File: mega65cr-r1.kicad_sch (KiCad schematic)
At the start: 0 parts

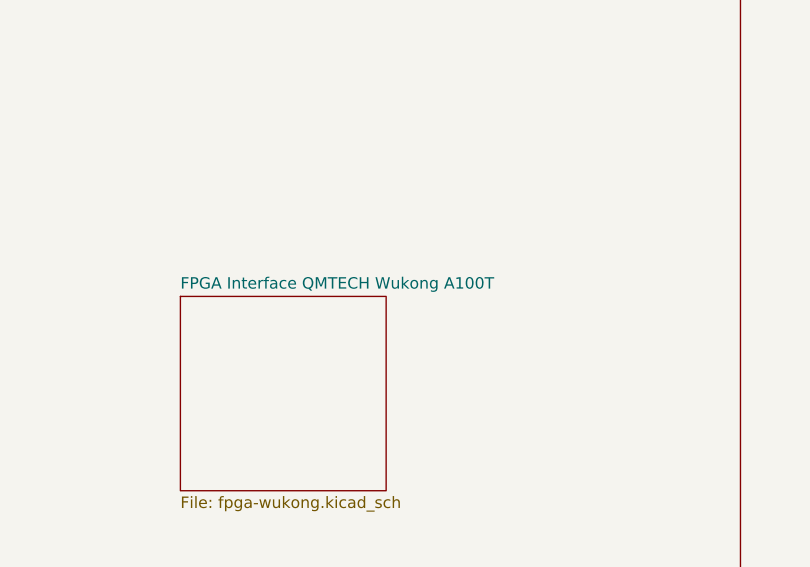
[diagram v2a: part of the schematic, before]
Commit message: add connectors and FPGA pin descriptions for QMTECH K345T board
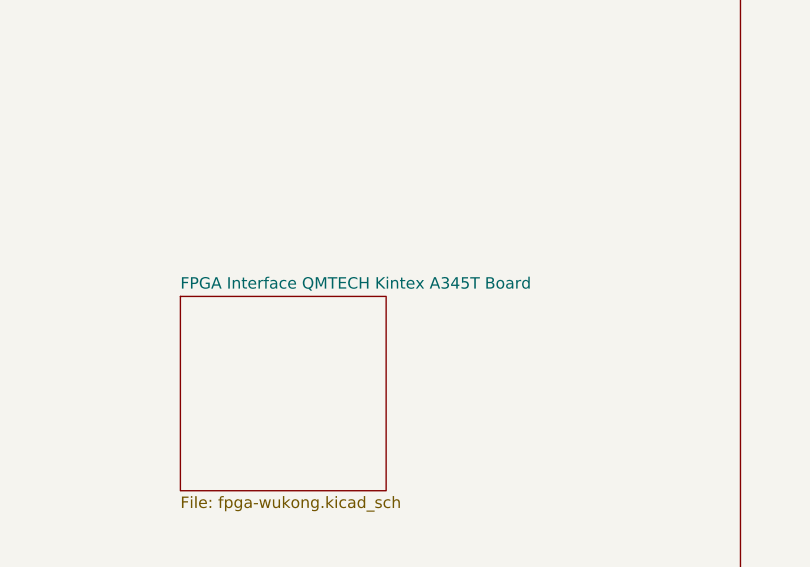
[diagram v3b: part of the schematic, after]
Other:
- sheet FPGA Interface QMTECH Wukong A100T renamed FPGA Interface QMTECH Kintex A345T Board
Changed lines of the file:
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@@
     (stroke (width 0.1524) (type solid) (color 0 0 0 0))
     (fill (color 0 0 0 0.0000))
-    (property "Sheet name" "FPGA Interface QMTECH Wukong A100T" (id 0) (at 104.14 74.2184 0)
+    (property "Sheet name" "FPGA Interface QMTECH Kintex A345T Board" (id 0) (at 104.14 74.2184 0)
       (effects (font (size 1.27 1.27)) (justify left bottom))
     )
@@
       (reference "J2") (unit 1) (value "DB9_Male_MountingHoles") (footprint "Connector_Dsub:DSUB-9_Male_Horizontal_P2.77x2.84mm_EdgePinOffset7.70mm_Housed_MountingHolesOffset9.12mm")
     )
+    (path "/2879178d-3b15-409b-b355-34424f0e3bd8/24d8d35c-436f-43c1-9f20-ff6b2f007989"
+      (reference "J4") (unit 1) (value "Conn_02x32_Odd_Even") (footprint "")
+    )
+    (path "/2879178d-3b15-409b-b355-34424f0e3bd8/4e0105b8-2efd-42c5-8acf-67155eec9ca7"
+      (reference "J5") (unit 1) (value "Conn_02x32_Odd_Even") (footprint "")
+    )
     (path "/bf6f0944-6234-4b84-bc75-6d48246ce101/9b2913aa-2e6f-4a94-a0c7-53573f96600d"

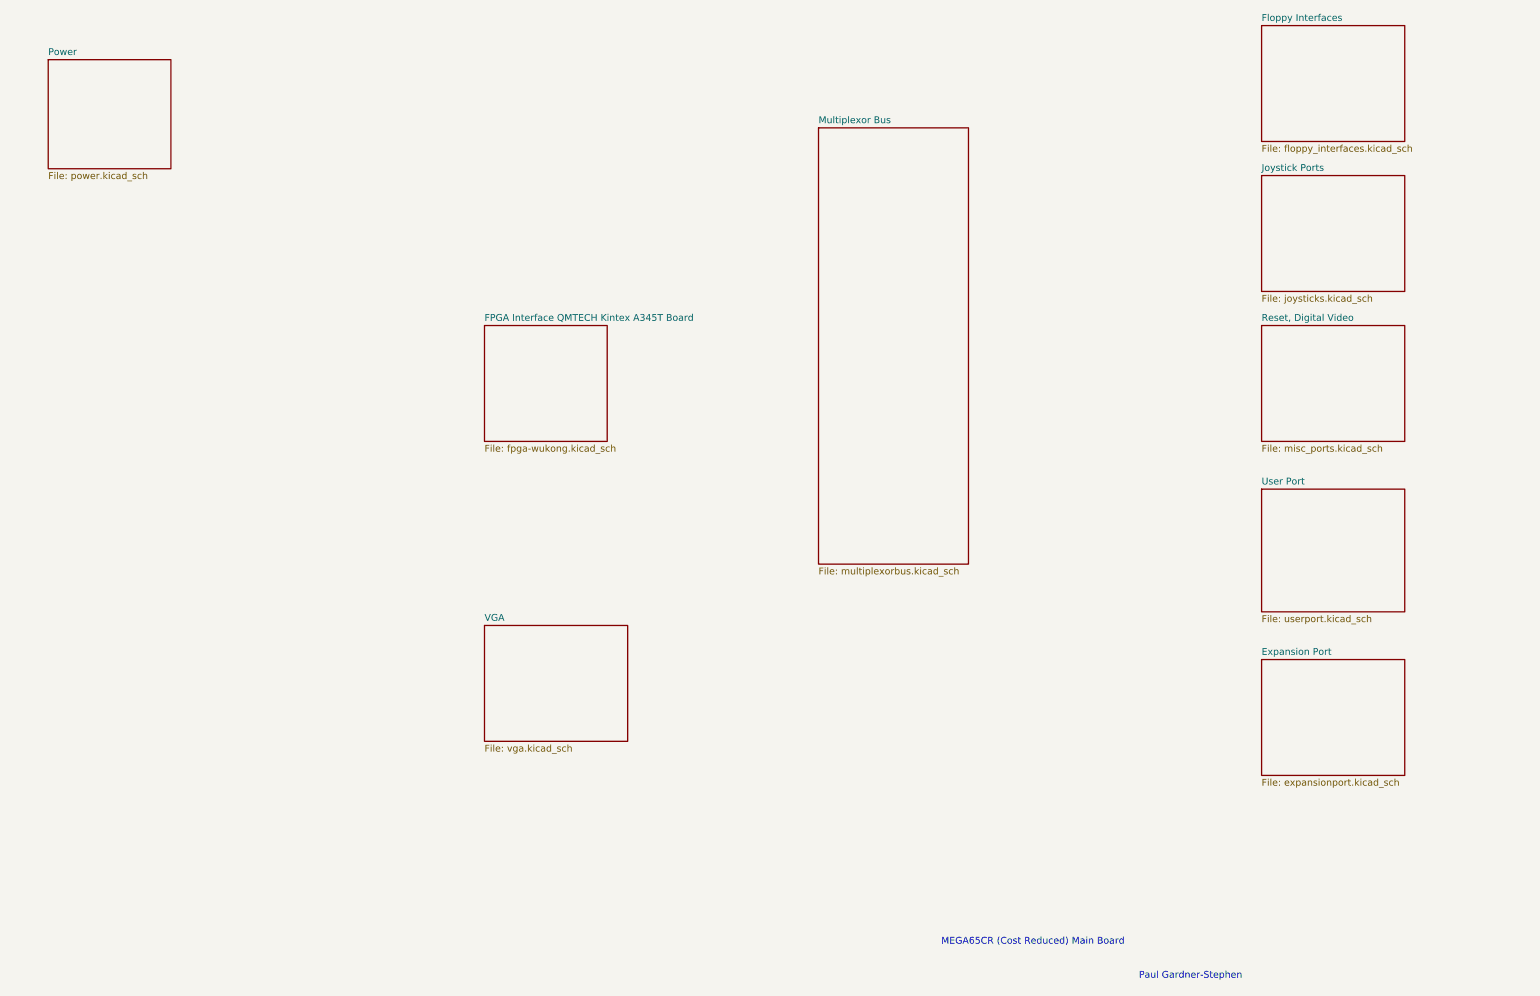
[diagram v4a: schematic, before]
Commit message: beautify the schematics, especially the title-page
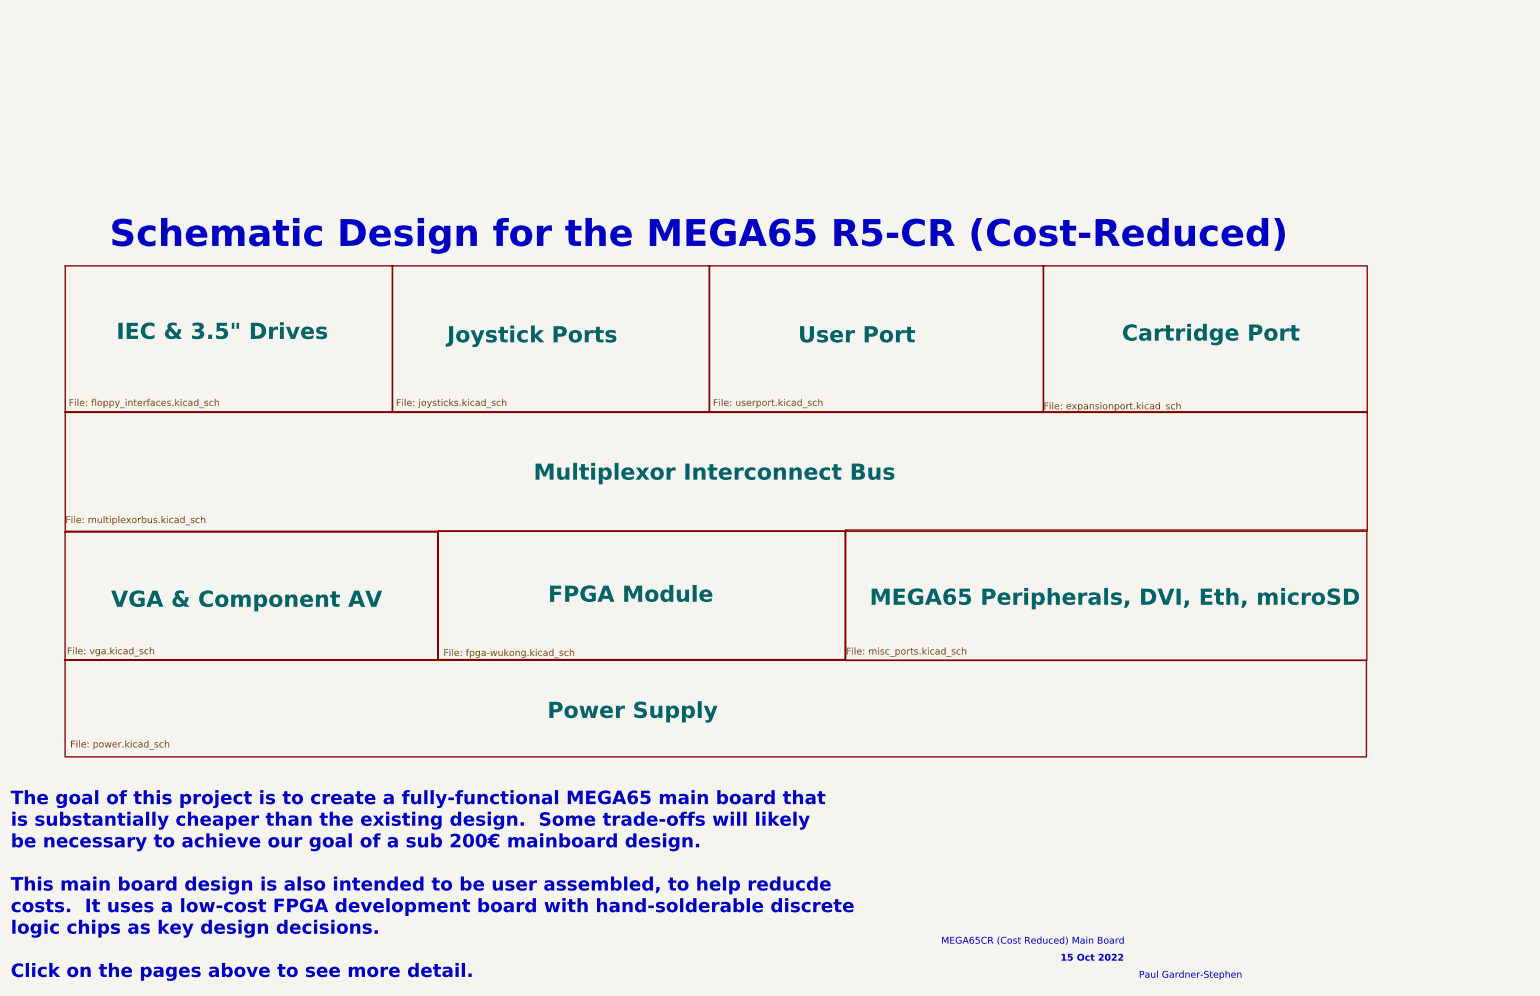
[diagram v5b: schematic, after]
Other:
- sheet Expansion Port renamed Cartridge Port
- sheet FPGA Interface QMTECH Kintex A345T Board renamed FPGA Module
- sheet Floppy Interfaces renamed IEC & 3.5" Drives
- sheet Multiplexor Bus renamed Multiplexor Interconnect Bus
- sheet Power renamed Power Supply
- sheet Reset, Digital Video renamed MEGA65 Peripherals, DVI, Eth, microSD
- sheet VGA renamed VGA & Component AV
- note added: "15 Oct 2022"
- note added: "Schematic Design for the MEGA65 R5-CR (Cost-Reduced)"
- note added: "The goal of this project is to create a fully-functional MEGA65 main board that is substantially cheaper than the existing design. Some trade-offs will likely be necessary to achieve our goal of a sub 200€ mainboard design. This main board design is also intended to be user assembled, to help reducde costs. It uses a low-cost FPGA development board with hand-solderable discrete logic chips as key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"
